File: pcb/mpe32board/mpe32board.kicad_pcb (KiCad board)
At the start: 4 copper layers, 98 x 79 mm, 224 parts, among them CN0295D LCD CN0295D, J1 Conn_ST_STDC14, J10 Conn_01x04, J11 Conn_01x04, J12 Conn_01x04, J13 Conn_01x04, J14 Conn_01x04, J15 Conn_01x04, J16 Conn_01x04, J17 Conn_01x04, J18 Conn_01x04, J19 Conn_01x04, J2 USB_C_Receptacle_USB2.0_16P, J20 Conn_01x04, J21 Conn_01x04, J22 Conn_01x04, J23 Conn_01x04, J24 Conn_01x04, J25 Conn_01x04, J26 Conn_01x04, J27 Conn_01x04, J3 Conn_01x01_Socket, J4 Conn_01x04, J44 Conn_01x05, J45 Conn_01x04_Socket, J46 Conn_02x10_Counter_Clockwise, J48 Micro_SD_Card_Det_Hirose_DM3AT, J49 AudioJack3_SwitchT, J5 Conn_01x04, J6 Conn_01x04, J7 Conn_01x04, J8 Conn_01x04, J9 Conn_01x04, SW1 SW_Push, SW2 SW_Push, SW3 SW_Push, SW4 SW_Push, SW5 SW_Push, SW6 SW_Push, U1 TAC5212IRGER, U10 W9812G6KH-75, U2 USBLC6-2P6, U3 AMS1117-3.3, U4 TCA9548ARGER, U5 TCA9548ARGER, U6 TCA9548ARGER, U9 STM32H743IITx

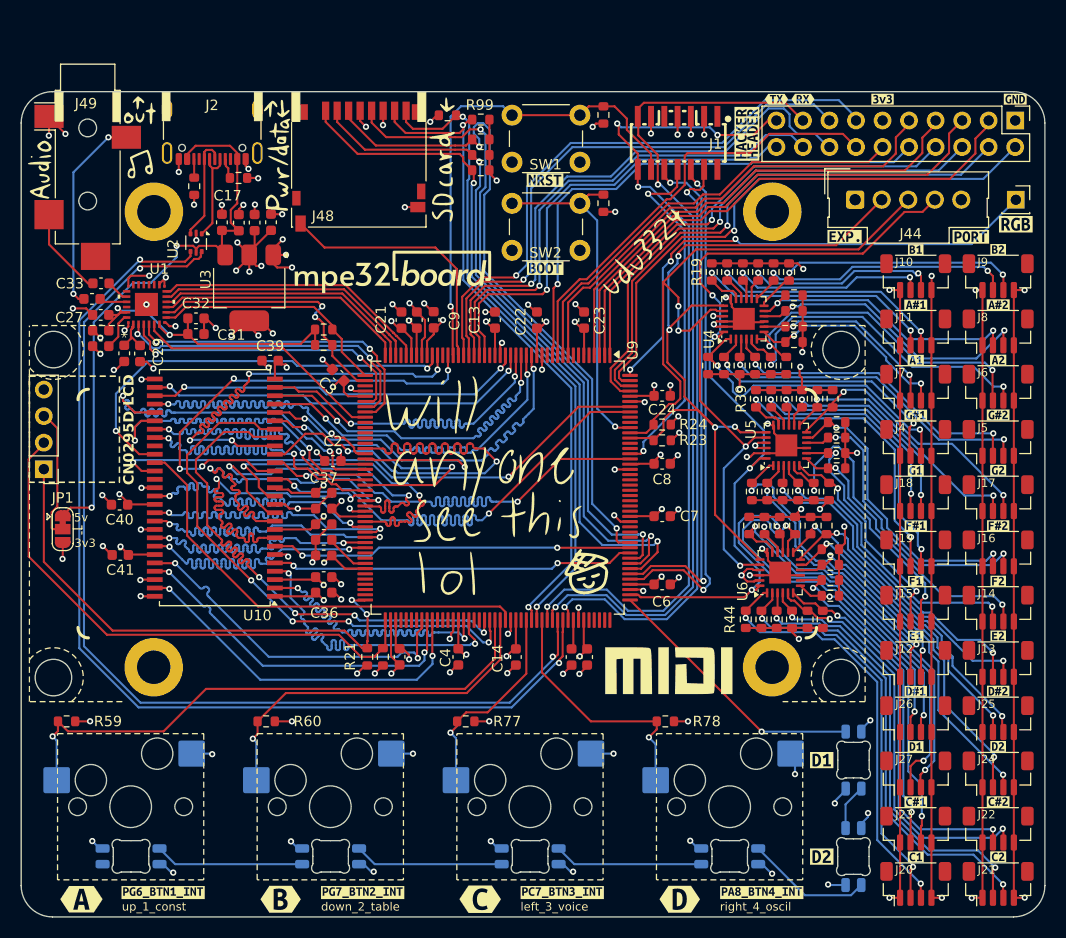
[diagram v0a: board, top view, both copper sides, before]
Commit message: add lcd level shifter, lm1117 ldo
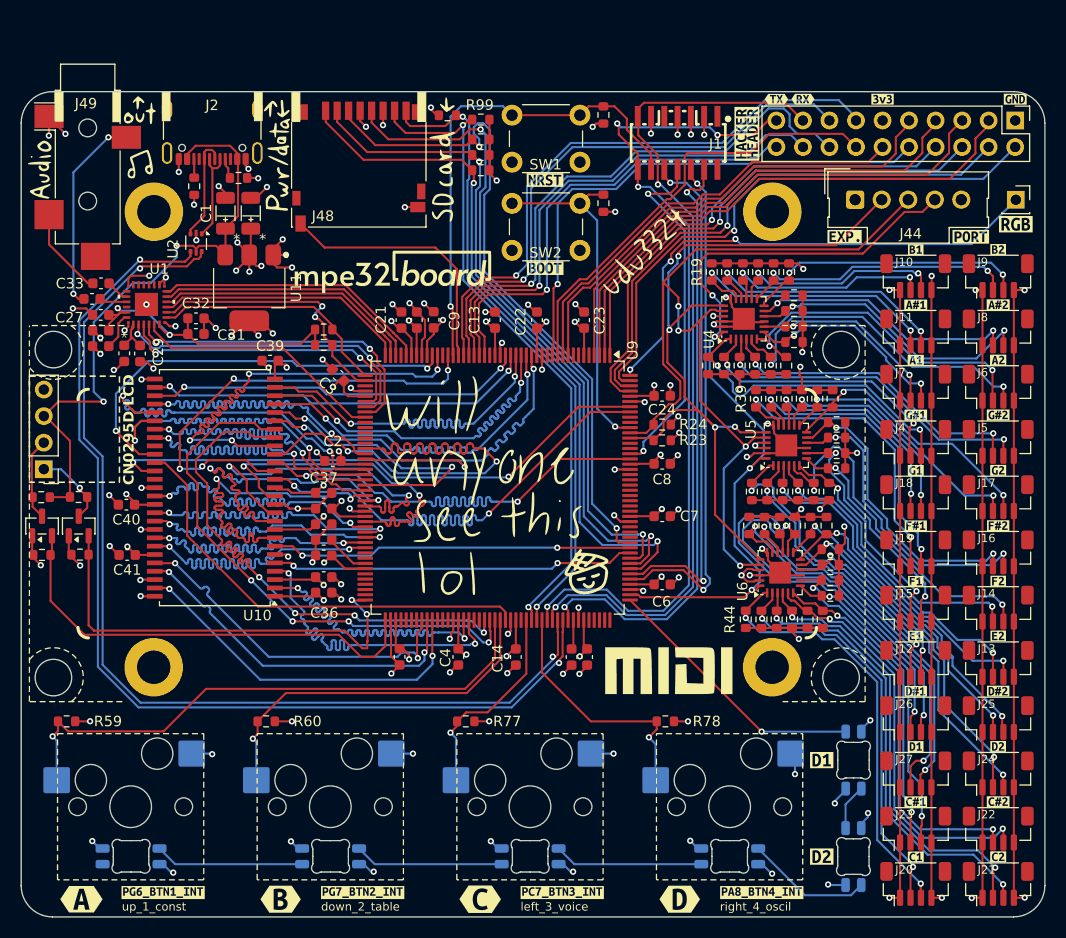
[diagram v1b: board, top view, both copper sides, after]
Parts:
- removed C17, C19: 10μF, Capacitor_SMD:C_0603_1608Metric
- removed C18, C20: 0.1μF, Capacitor_SMD:C_0603_1608Metric
- removed JP1: SolderJumper_3_Bridged12, Jumper:SolderJumper-3_P1.3mm_Bridged12_RoundedPad1.0x1.5mm
- removed U3: AMS1117-3.3, Package_TO_SOT_SMD:SOT-223-3_TabPin2
- added C1: 10μF, Capacitor_SMD:C_1206_3216Metric, F.Cu at (79.6, 91.6)
- added C42: 10μF, Capacitor_SMD:C_1206_3216Metric, F.Cu at (82.0, 91.6)
- added Q1: BSS138, Package_TO_SOT_SMD:SOT-23, F.Cu at (65.5, 121.6)
- added Q2: BSS138, Package_TO_SOT_SMD:SOT-23, F.Cu at (62.0, 121.6)
- added R100: 10kΩ, Resistor_SMD:R_0603_1608Metric, F.Cu at (62.0, 124.3)
- added R101: 10kΩ, Resistor_SMD:R_0603_1608Metric, F.Cu at (61.9, 118.8)
- added U11: LM1117MP-3.3, Package_TO_SOT_SMD:SOT-223-3_TabPin2, F.Cu at (81.8, 98.8)
- moved R22 32.9 mm to (65.5, 118.8), turned to 180 degrees
- moved R21 29.2 mm to (65.6, 124.3), turned to 0 degrees
- moved C41 0.66 mm to (70.2, 124.3)
- moved C40 0.66 mm to (70.1, 119.5)
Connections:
- J45 pad 1: I2C4_SCL -> I2C4_SCL_5V
- J45 pad 2: I2C4_SDA -> I2C4_SDA_5V
- J45 pad 3: Net-(J45-Pin_3) -> +5V
- R21 pad 1: I2C4_SCL -> +3V3
- R21 pad 2: +3V3 -> I2C4_SCL
- R22 pad 1: I2C4_SDA -> I2C4_SCL_5V
- R22 pad 2: +3V3 -> +5V
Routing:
- net Net-(J45-Pin_3): track 12.5 -> 0.00 mm
- net I2C4_SDA: track 52.6 -> 43.4 mm
- net I2C4_SDA_5V: track 0.00 -> 7.92 mm
- net I2C4_SCL_5V: track 0.00 -> 7.73 mm, vias 0 -> 1
- net I2C4_SCL: track 49.9 -> 42.8 mm
- net +5V: track 56.1 -> 58.8 mm
- net +3V3: track 356.4 -> 355.3 mm, vias 68 -> 67
- net GND: track 289.0 -> 288.3 mm, vias 93 -> 91
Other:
- board text added: "*"
- board text removed: "3v3"
- board text removed: "5v"

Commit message: fix power scheme and add usb diode + more
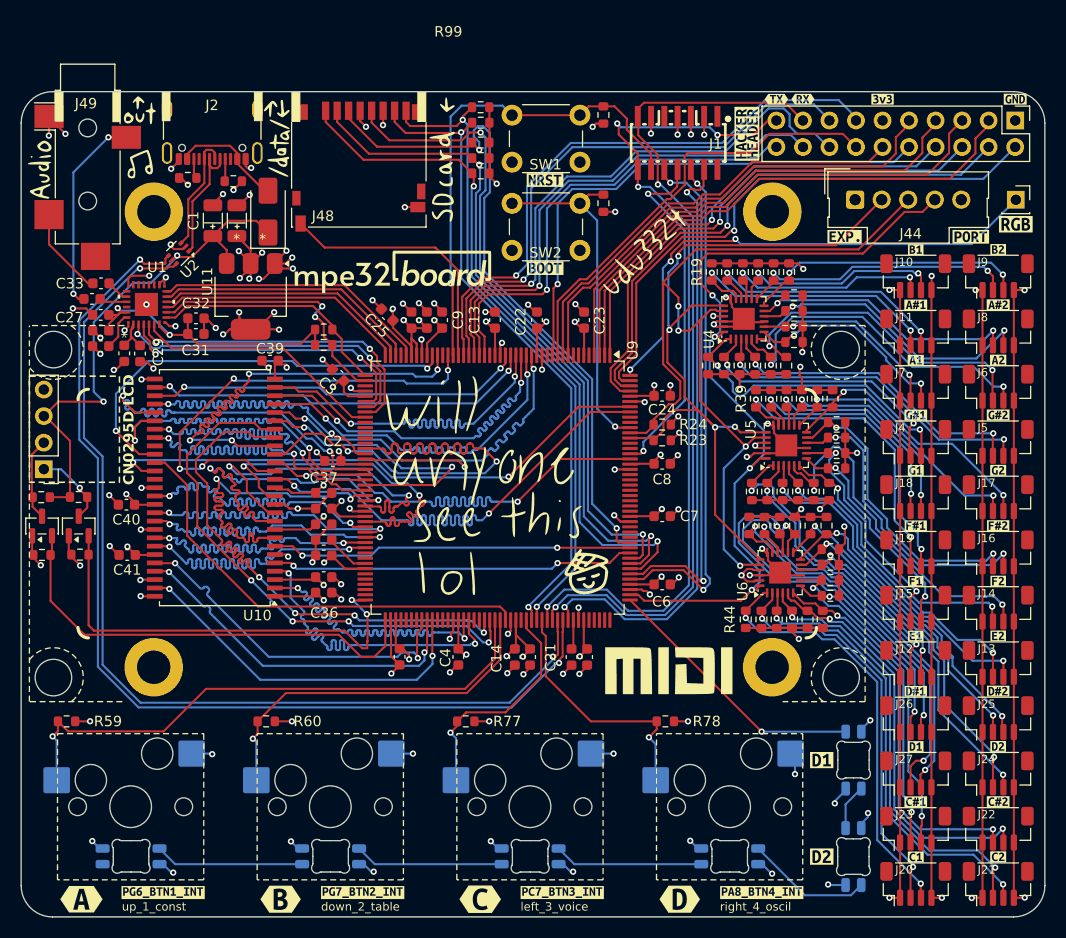
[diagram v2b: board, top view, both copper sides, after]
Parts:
- added C17: 100nF, Capacitor_SMD:C_0603_1608Metric, F.Cu at (97.4, 101.9)
- added C43: 1μF, Capacitor_SMD:C_0603_1608Metric, F.Cu at (98.8, 101.9)
- added D1: SS14, Diode_SMD:D_SMA, F.Cu at (83.6, 91.5)
- moved C21 34.5 mm to (108.7, 134.1), turned to -90 degrees
- moved R99 3.27 mm to (104.0, 81.5), turned to 180 degrees
- moved C25 2.88 mm to (95.0, 101.4), turned to 135 degrees
- moved U2 1.96 mm to (75.1, 95.5), turned to -135 degrees
- moved C42 1.51 mm to (80.7, 92.3)
- moved C1 1.40 mm to (78.3, 92.3)
- moved R4 1.01 mm to (76.0, 88.3), turned to 180 degrees
- moved U11 0.83 mm to (82.0, 99.6)
- moved C9 0.81 mm to (100.3, 101.9)
- moved R3 0.59 mm to (80.3, 88.6)
- moved R95 0.30 mm to (104.0, 84.9)
- moved R96 0.30 mm to (104.0, 87.8)
- moved R97 0.30 mm to (104.0, 86.4)
- moved R98 0.30 mm to (104.0, 83.0)
- moved C14 0.10 mm to (107.3, 134.1)
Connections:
- J2 pad A4: +5V -> Net-(D1-A)
- J2 pad A9: +5V -> Net-(D1-A)
- J2 pad B4: +5V -> Net-(D1-A)
- J2 pad B9: +5V -> Net-(D1-A)
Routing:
- net +3V3: track 355.3 -> 371.1 mm, vias 67 -> 69
- net Net-(D1-A): track 0.00 -> 11.0 mm
- net +5V: track 58.8 -> 50.2 mm
- net GND: track 288.3 -> 291.7 mm, vias 91 -> 95
- net OTG_FS_DN: track 98.3 -> 95.2 mm
- net Net-(J2-D--PadA7): track 9.14 -> 12.1 mm
- net BTN3_INTERNAL: track 19.8 -> 21.9 mm
- net OTG_FS_DP: track 99.6 -> 97.5 mm
- net Net-(J2-D+-PadA6): track 10.2 -> 11.5 mm
- net SDMMC1_D1: track 61.5 -> 62.4 mm

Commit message: remove production files
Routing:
- net I2C4_SCL: track 42.8 -> 39.4 mm
- net I2C4_SDA: track 43.4 -> 40.3 mm
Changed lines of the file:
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@@
 	)
 	(segment
-		(start 91.65 128.66)
-		(end 91.7 128.71)
-		(width 0.2)
-		(layer "F.Cu")
-		(net "I2C4_SCL")
-	)
-	(segment
-		(start 90.96 131.591691)
+		(start 66.455 131.085)
 		(end 66.961691 131.591691)
 		(width 0.2)
@@
 	)
 	(segment
-		(start 92.885 128.71)
-		(end 92.935 128.66)
+		(start 91.518309 131.591691)
+		(end 93.09 130.02)
 		(width 0.2)
 		(layer "F.Cu")
@@
 	)
 	(segment
-		(start 93.16 130.09)
-		(end 93.16 132.6)
-		(width 0.2)
-		(layer "F.Cu")
-		(net "I2C4_SCL")
-	)
-	(segment
-		(start 93.16 132.6)
-		(end 93.13 132.63)
+		(start 91.65 128.66)
+		(end 91.7 128.71)
 		(width 0.2)
 		(layer "F.Cu")
@@
 	)
 	(segment
-		(start 66.455 131.085)
-		(end 66.455 124.32)
+		(start 66.961691 131.591691)
+		(end 91.518309 131.591691)
 		(width 0.2)
 		(layer "F.Cu")
@@
 	)
 	(segment
-		(start 66.961691 131.591691)
-		(end 66.455 131.085)
+		(start 92.885 128.71)
+		(end 92.935 128.66)
 		(width 0.2)
 		(layer "F.Cu")
@@
 	)
 	(segment
-		(start 93.13 133.278669)
-		(end 92.646978 133.278669)
-		(width 0.2)
-		(layer "F.Cu")
-		(net "I2C4_SCL")
-	)
-	(segment
-		(start 93.13 132.63)
-		(end 93.13 133.278669)
+		(start 66.455 124.32)
+		(end 66.455 131.085)
 		(width 0.2)
 		(layer "F.Cu")
@@
 	)
 	(segment
-		(start 93.09 130.02)
-		(end 93.16 130.09)
-		(width 0.2)
-		(layer "F.Cu")
-		(net "I2C4_SCL")
-	)
-	(segment
 		(start 66.46 124.315)
 		(end 66.455 124.32)
@@
 		(net "I2C4_SCL")
 	)
-	(segment
-		(start 92.646978 133.278669)
-		(end 90.96 131.591691)
-		(width 0.2)
-		(layer "F.Cu")
-		(net "I2C4_SCL")
-	)
 	(via
 		(at 93.09 130.02)
@@
 	)
 	(segment
-		(start 66.061691 131.991691)
-		(end 90.421691 131.991691)
-		(width 0.2)
-		(layer "F.Cu")
-		(net "I2C4_SDA")
-	)
-	(segment
 		(start 62.95 122.5175)
 		(end 62.95 124.215)
@@
 	)
 	(segment
-		(start 93.808669 134.1)
-		(end 94.63 133.278669)
-		(width 0.2)
-		(layer "F.Cu")
-		(net "I2C4_SDA")
-	)
-	(segment
-		(start 90.421691 131.991691)
-		(end 92.53 134.1)
-		(width 0.2)
-		(layer "F.Cu")
-		(net "I2C4_SDA")
-	)
-	(segment
-		(start 94.86 133.078669)
-		(end 94.66 133.278669)
-		(width 0.2)
-		(layer "F.Cu")
-		(net "I2C4_SDA")
-	)
-	(segment
-		(start 94.86 130.585)
-		(end 94.86 133.078669)
+		(start 93.453309 131.991691)
+		(end 94.86 130.585)
 		(width 0.2)
 		(layer "F.Cu")
@@
 	)
 	(segment
-		(start 62.815 124.35)
-		(end 62.815 128.745)
+		(start 62.815 128.745)
+		(end 66.061691 131.991691)
 		(width 0.2)
 		(layer "F.Cu")
@@
 	)
 	(segment
-		(start 92.53 134.1)
-		(end 93.808669 134.1)
+		(start 66.061691 131.991691)
+		(end 93.453309 131.991691)
 		(width 0.2)
 		(layer "F.Cu")
@@
 	)
 	(segment
-		(start 62.815 128.745)
-		(end 66.061691 131.991691)
+		(start 62.815 124.35)
+		(end 62.815 128.745)
 		(width 0.2)
 		(layer "F.Cu")
@@
 	)
 	(segment
+		(start 80.69 86.45)
+		(end 80.76 86.52)
+		(width 0.2)
+		(layer "F.Cu")
+		(net "Net-(D1-A)")
+	)
+	(segment
+		(start 80.69 86.885686)
+		(end 83.286814 89.4825)
+		(width 0.2)
+		(layer "F.Cu")
+		(net "Net-(D1-A)")
+	)
+	(segment
+		(start 79.989999 85.175)
+		(end 76.705 85.175)
+		(width 0.2)
+		(layer "F.Cu")
+		(net "Net-(D1-A)")
+	)
+	(segment
+		(start 80.69 85.875001)
+		(end 79.989999 85.175)
+		(width 0.2)
+		(layer "F.Cu")
+		(net "Net-(D1-A)")
+	)
+	(segment
+		(start 75.89 85.99)
+		(end 75.89 86.45)
+		(width 0.2)
+		(layer "F.Cu")
+		(net "Net-(D1-A)")
+	)
+	(segment
+		(start 80.69 86.45)
+		(end 80.69 85.875001)
+		(width 0.2)
+		(layer "F.Cu")
+		(net "Net-(D1-A)")
+	)
+	(segment
+		(start 80.69 86.45)
+		(end 80.69 86.885686)
+		(width 0.2)
+		(layer "F.Cu")
+		(net "Net-(D1-A)")
+	)
+	(segment
+		(start 76.705 85.175)
+		(end 75.89 85.99)
+		(width 0.2)
+		(layer "F.Cu")
+		(net "Net-(D1-A)")
+	)
+	(segment
+		(start 83.286814 89.4825)
+		(end 83.63 89.4825)
+		(width 0.2)
+		(layer "F.Cu")
+		(net "Net-(D1-A)")
+	)
+	(segment
 		(start 132.0025 115.8)
 		(end 131.6075 115.8)
@@
 		(net "Net-(D5-DOUT)")
 	)
-	(segment
-		(start 80.69 86.45)
-		(end 80.76 86.52)
-		(width 0.2)
-		(layer "F.Cu")
-		(net "Net-(D1-A)")
-	)
-	(segment
-		(start 80.69 86.885686)
-		(end 83.286814 89.4825)
-		(width 0.2)
-		(layer "F.Cu")
-		(net "Net-(D1-A)")
-	)
-	(segment
-		(start 79.989999 85.175)
-		(end 76.705 85.175)
-		(width 0.2)
-		(layer "F.Cu")
-		(net "Net-(D1-A)")
-	)
-	(segment
-		(start 80.69 85.875001)
-		(end 79.989999 85.175)
-		(width 0.2)
-		(layer "F.Cu")
-		(net "Net-(D1-A)")
-	)
-	(segment
-		(start 75.89 85.99)
-		(end 75.89 86.45)
-		(width 0.2)
-		(layer "F.Cu")
-		(net "Net-(D1-A)")
-	)
-	(segment
-		(start 80.69 86.45)
-		(end 80.69 85.875001)
-		(width 0.2)
-		(layer "F.Cu")
-		(net "Net-(D1-A)")
-	)
-	(segment
-		(start 80.69 86.45)
-		(end 80.69 86.885686)
-		(width 0.2)
-		(layer "F.Cu")
-		(net "Net-(D1-A)")
-	)
-	(segment
-		(start 76.705 85.175)
-		(end 75.89 85.99)
-		(width 0.2)
-		(layer "F.Cu")
-		(net "Net-(D1-A)")
-	)
-	(segment
-		(start 83.286814 89.4825)
-		(end 83.63 89.4825)
-		(width 0.2)
-		(layer "F.Cu")
-		(net "Net-(D1-A)")
-	)
 	(zone
